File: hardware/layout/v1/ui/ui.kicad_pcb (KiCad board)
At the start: 2 copper layers, 49.5 x 40.5 mm, 18 parts, among them J1 JST-SH 1x10, J2 OLED, SW1 PRG/RST, SW2 FUNC, U1 74AHCT1G125

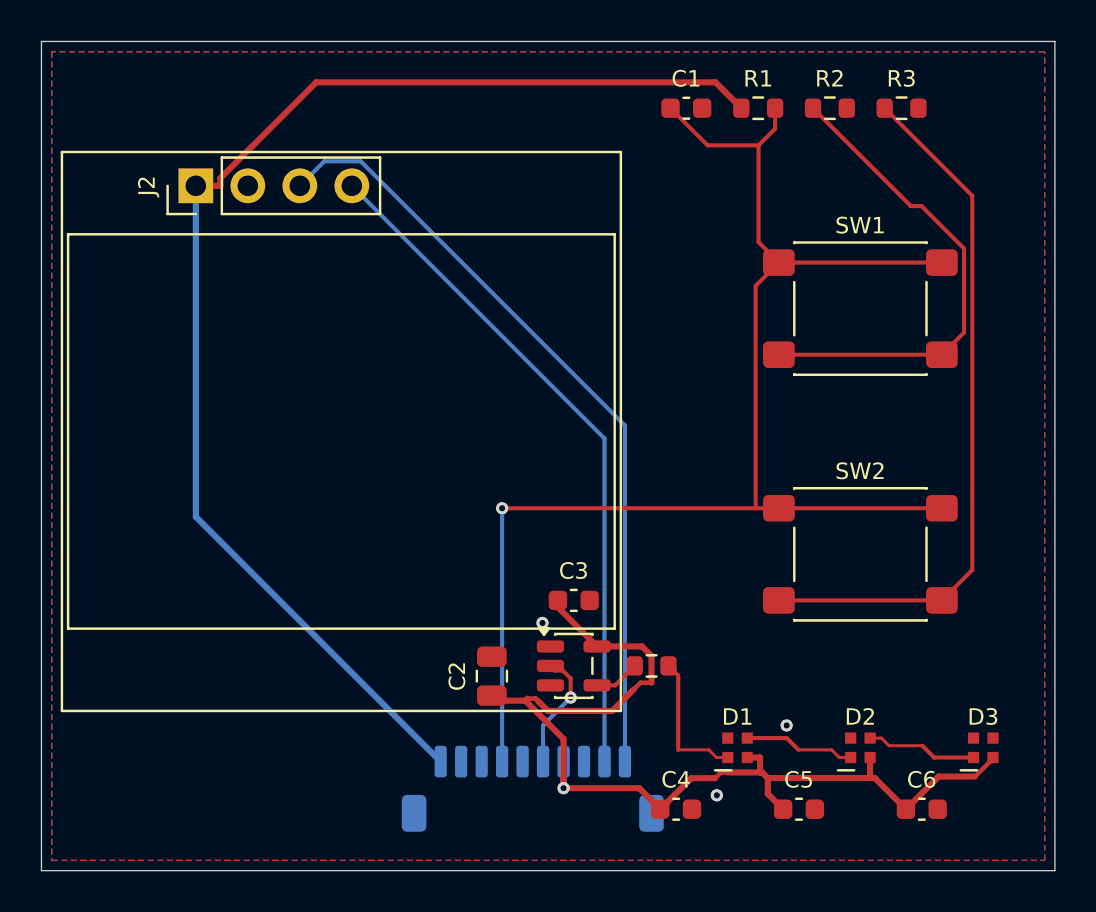
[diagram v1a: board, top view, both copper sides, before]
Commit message: V3 consolidated to two boards (main + ui); updated firmware pin map, button ADC, and OLED connector; removed separate knx/dali boards from CI matrix
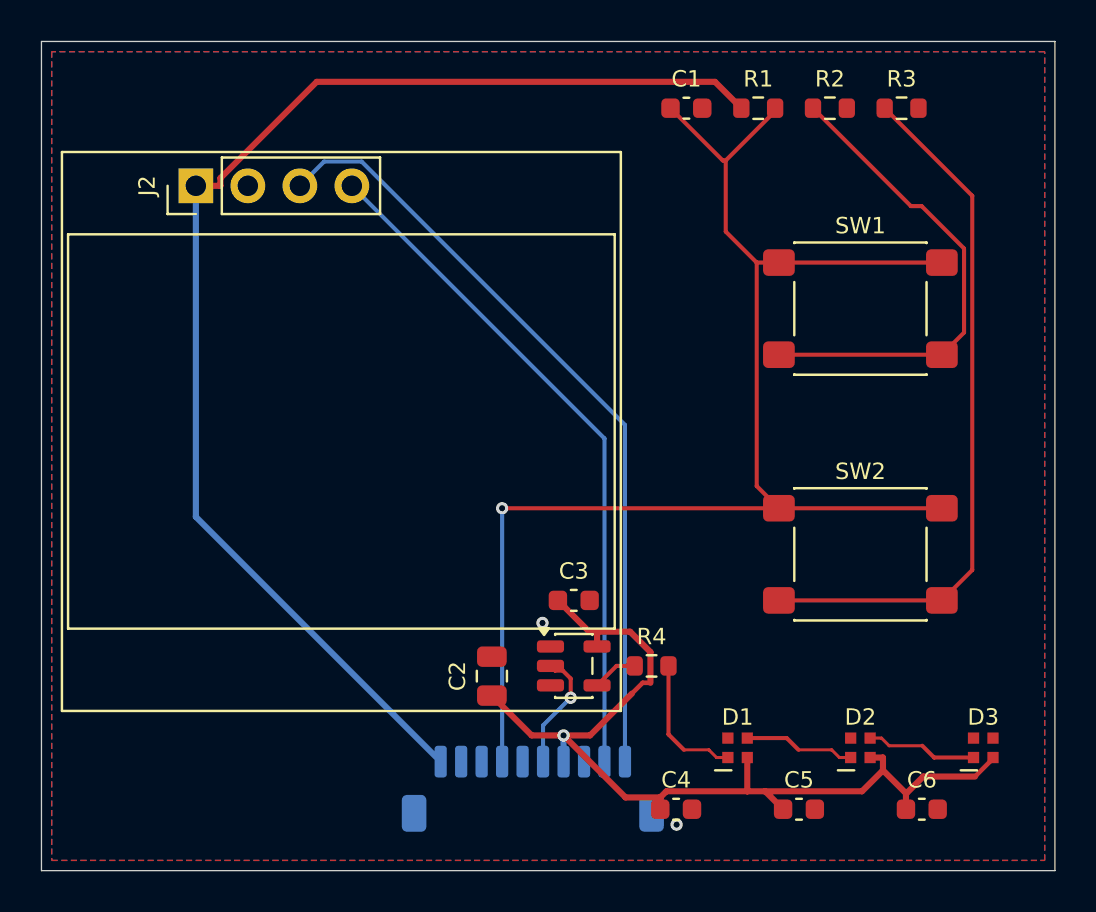
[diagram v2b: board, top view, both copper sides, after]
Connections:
- J1 pad 8: LED_DALI -> GND
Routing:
- net +5V: track 50.5 -> 48.2 mm
- net BTN_LADDER: track 67.6 -> 68.3 mm
- net GND: vias 3 -> 2
